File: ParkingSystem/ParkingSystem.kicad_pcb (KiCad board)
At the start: 2 copper layers, 55.9 x 64.1 mm, 45 parts, among them J1 PJ-002A, J2 0430450400, J3 Conn_ARM_JTAG_SWD_10, J4 Conn_01x04_Female, J5 0430450200, Q1 SSM3K333R,LF, Q2 SSM3K333R,LF, Q3 SSM3K333R,LF, Q4 SSM3K333R,LF, Q5 SSM3K333R,LF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

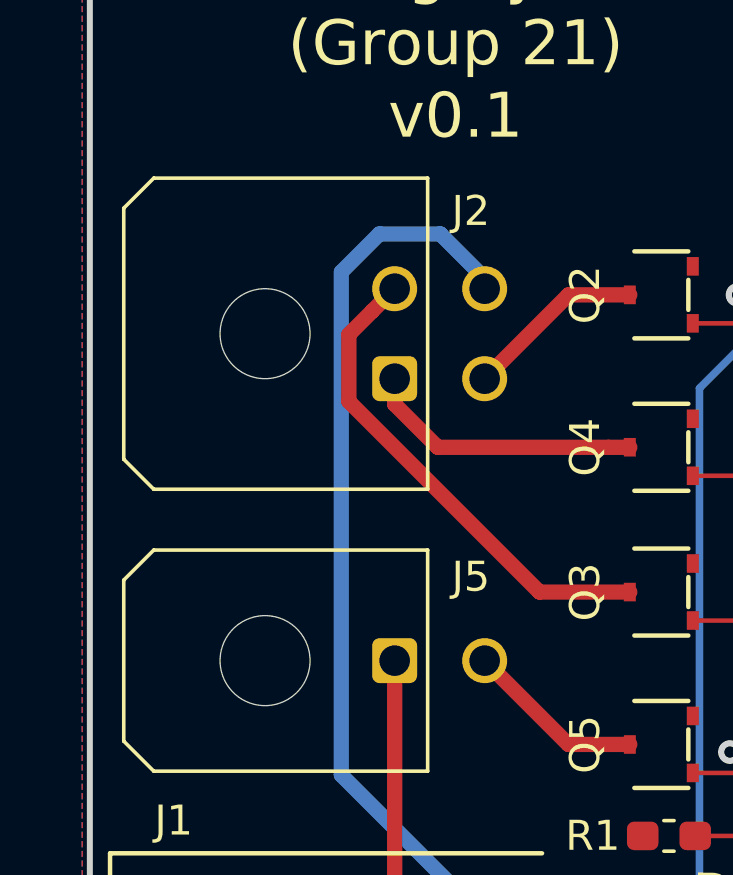
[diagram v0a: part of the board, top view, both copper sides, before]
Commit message: Add few 3D Bodies, and more dimensions
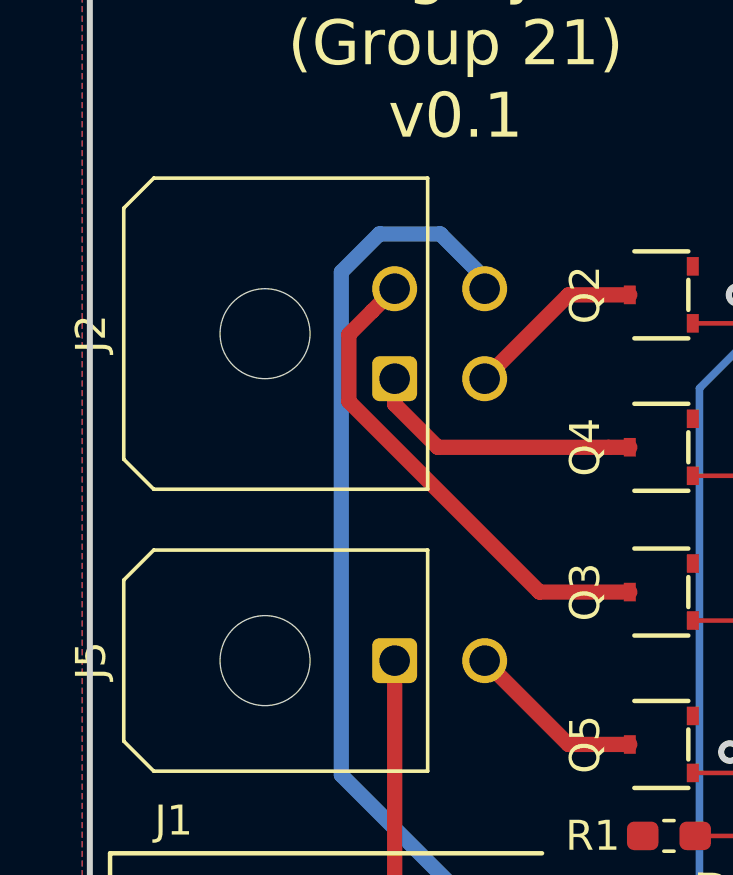
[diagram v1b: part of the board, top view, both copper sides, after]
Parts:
- J2: footprint Connector_Molex:Molex_Micro-Fit_3.0_43045-0400_2x02_P3.00mm_Horizontal -> Connectors:Molex_Micro-Fit_3.0_43045-0400_2x02_P3.00mm_Horizontal
- J5: footprint Connector_Molex:Molex_Micro-Fit_3.0_43045-0200_2x01_P3.00mm_Horizontal -> Connectors:Molex_Micro-Fit_3.0_43045-0200_2x01_P3.00mm_Horizontal
